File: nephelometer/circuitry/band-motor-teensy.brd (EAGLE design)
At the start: 77 x 48 mm, 25 parts, among them IC3 7805TV, J1 2.1MMJACKTHM, U1 MotA, U2 MotA

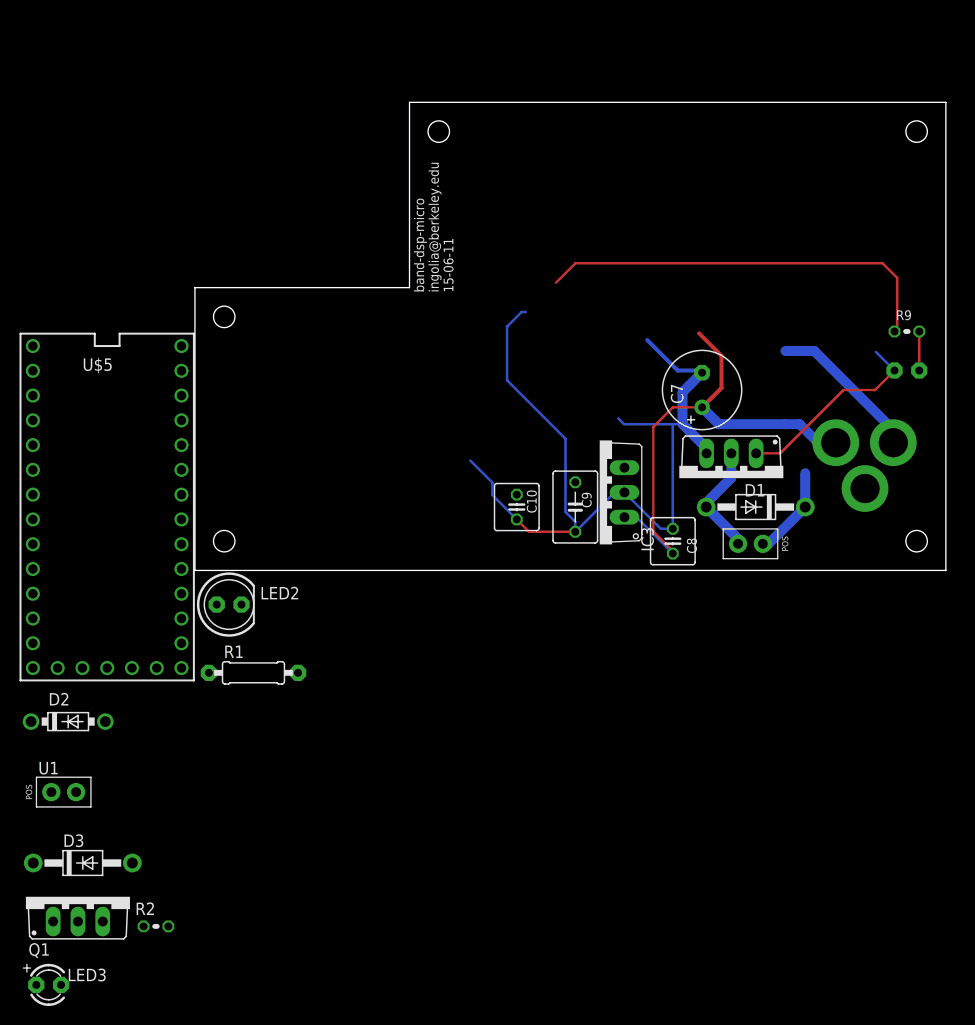
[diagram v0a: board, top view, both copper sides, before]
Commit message: Designed motor power board to stack on nephelometer or run over RJ11 cable
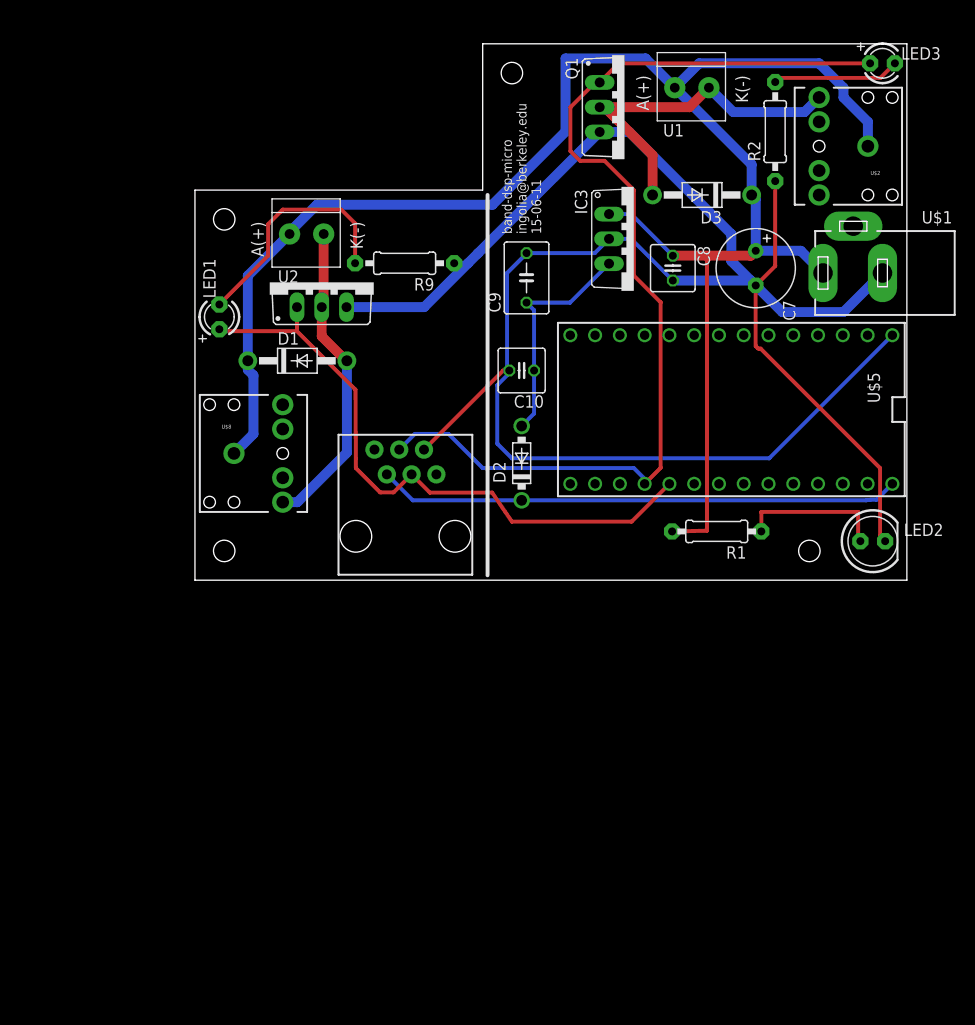
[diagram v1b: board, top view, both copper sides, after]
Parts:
- added U$6: (no value), ingolia:M2MOUNT
- added U$8: AUDIO-JACK2PTH, SparkFun-Connectors:AUDIO-JACK
- J1: value 2.1MMJACKTHM -> RJ11-6PTH; device adafruit:PJ-102A -> SparkFun-Connectors:RJ11-6
- R2, R9: device adafruit:0204V -> adafruit:0207/10
- U$1: value (none) -> PJ-102A; device ingolia:M2MOUNT -> ingolia:PJ-102A
- U$2: value (none) -> AUDIO-JACK2PTH; device ingolia:M2MOUNT -> SparkFun-Connectors:AUDIO-JACK
- U$5: value TEENSY_3.1-3.2_OUTER_ROW -> TEENSY_3.1-3.2_DIL; device Teensy_3_and_LC_Series_Boards_v1.4:TEENSY_3.0-3.2&LC_OUTER_ROW -> Teensy_3_and_LC_Series_Boards_v1.4:TEENSY_3.0-3.2&LC_DIL
- U1, U2: device ingolia:1X02_SCREW -> ingolia:1X02_3.5MM_MOT
- moved LED3 127.4 mm to (70.5, 58.0)
- moved R2 103.3 mm to (59.5, 51.0), turned to 90 degrees
- moved U1 99.5 mm to (51.0, 55.5), turned to 180 degrees
- moved Q1 99.2 mm to (41.5, 53.5), turned to 270 degrees
- moved D3 93.4 mm to (52.0, 44.5), turned to 180 degrees
- moved U$3 71.0 mm to (3.00, 8.00)
- moved LED1 70.7 mm to (2.50, 32.0), flipped to the top, turned to 90 degrees
- moved U$1 70.1 mm to (67.5, 36.5), turned to 90 degrees
- moved LED2 66.3 mm to (69.5, 9.00)
- moved U$5 64.8 mm to (55.0, 22.5), turned to 270 degrees
- moved J1 59.3 mm to (16.5, 9.50), flipped to the top, turned to 0 degrees
- moved U$7 57.4 mm to (63.0, 8.00)
- moved U2 56.9 mm to (11.5, 40.5)
- moved D2 53.5 mm to (33.5, 17.0), turned to 90 degrees
- moved R9 52.0 mm to (21.5, 37.5), turned to 180 degrees
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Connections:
- removed net N$19: LED1.A, Q3.G, U$5.17/A3
- removed net N$6: LED3.A, Q1.G, U$5.16/A2
- removed net VBAT: U$5.VBAT
- new net MOT1: J1.3, LED3.A, Q1.G, U$5.16/A2
- new net MOT2: J1.4, LED1.A, Q3.G, U$5.17/A3
- net +12V: now also U$1.1TIP, U$2.SLEEVE, U$8.SLEEVE, U1.1A, U2.1A; no longer J1.TIP, U1.1/POS, U2.1/POS
- net +5V: now also J1.2
- net 3.3V: no longer U$5.3.3V1
- net GND: now also J1.5, U$1.3RING; no longer J1.RING, U$5.GND1
- net N$3: now also U$8.TIP, U2.2K; no longer U2.2
- net N$4: now also U$2.TIP, U1.2K; no longer U1.2
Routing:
- net +12V: track 58.3 -> 181.3 mm
- net MOT1: track 0.00 -> 105.4 mm
- net GND: track 147.3 -> 222.9 mm
- net MOT2: track 0.00 -> 64.9 mm
- net +5V: track 0.00 -> 53.6 mm
- net N$4: track 0.00 -> 36.0 mm
- net N$2: track 0.00 -> 23.6 mm
- net N$3: track 11.7 -> 32.8 mm
- net N$16: track 4.00 -> 24.5 mm
- net N$19: track 20.4 -> 0.00 mm
- net N$1: track 0.00 -> 15.2 mm
- net N$5: track 0.00 -> 13.1 mm
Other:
- board size 77 x 48 mm -> 73 x 55 mm

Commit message: Motor control with transistor gating MOSFET, shutoff when disconnected
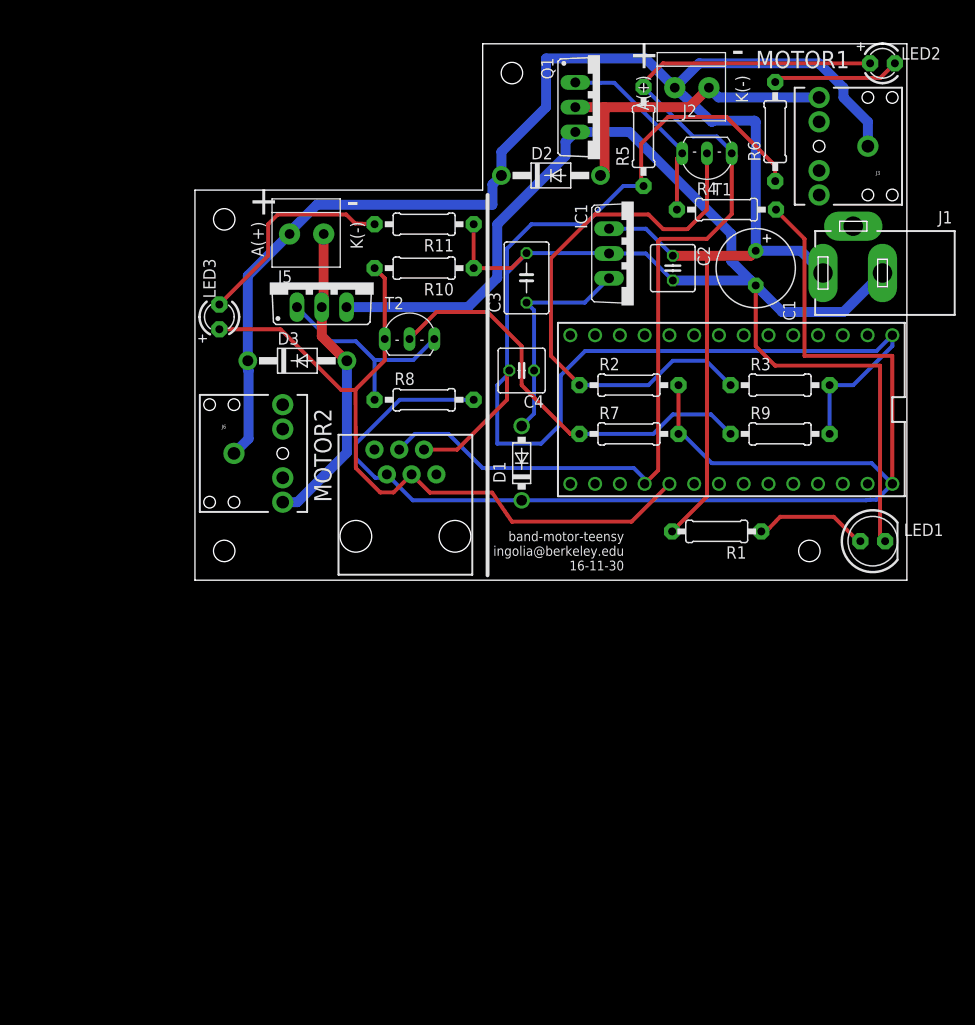
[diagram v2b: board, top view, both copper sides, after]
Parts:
- removed IC3: 7805TV, linear:TO220V
- removed U$1: PJ-102A, ingolia:PJ-102A
- added IC1: 7805TV, linear:TO220V
- added J4: RJ11-6PTH, SparkFun-Connectors:RJ11-6
- added R10, R3, R5, R7: 1K0, adafruit:0207/10
- added R11, R6: 150R, adafruit:0207/10
- added R4, R8: 4K7, adafruit:0207/10
- added T1, T2: 2N2222, adafruit:TO92-EBC-OVAL
- D1: value 1N4935 -> 1N5817-T; device adafruit:DO41-10 -> diode:DO41-7.6
- D2: value 1N5817-T -> 1N4935; device diode:DO41-7.6 -> adafruit:DO41-10
- J1: value RJ11-6PTH -> PJ-102A; device SparkFun-Connectors:RJ11-6 -> ingolia:PJ-102A
- LED1: device adafruit:LED3MM -> adafruit:LED5MM
- LED2: device adafruit:LED5MM -> adafruit:LED3MM
- R2, R9: value 150 -> 1K0
- moved LED3 72.8 mm to (2.50, 32.0), turned to 90 degrees
- moved LED1 70.8 mm to (69.5, 9.00), turned to 0 degrees
- moved J1 57.7 mm to (67.5, 36.5), turned to 90 degrees
- moved LED2 49.0 mm to (70.5, 58.0)
- moved D3 44.8 mm to (10.5, 27.5), turned to 0 degrees
- moved R9 42.3 mm to (60.0, 20.0), turned to 0 degrees
- moved R2 30.0 mm to (44.5, 25.0), turned to 0 degrees
- moved D2 29.7 mm to (36.5, 46.5), turned to 0 degrees
- moved D1 25.3 mm to (33.5, 17.0), turned to 90 degrees
- moved Q1 2.50 mm to (39.0, 53.5)
- renumbered C10 to C4, C7 to C1, C8 to C2, C9 to C3, Q3 to Q2, U$2 to J3, U$5 to MCU1, U$8 to J6, U1 to J2, U2 to J5
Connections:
- new net N$6: R2.1, R3.1, T1.B
- new net N$7: R7.1, R9.1, T2.B
- new net N$8: Q1.G, R4.1, T1.C
- new net N$9: Q2.G, R8.1, T2.C
- net +12V: now also D2.C, IC1.1, J1.1TIP; no longer D1.C, IC3.1, U$1.1TIP
- net +5V: now also D1.C, J4.2, R2.2, R4.2, R7.2, R8.2; no longer D2.C, J1.2
- net GND: now also IC1.2, J1.3RING, J4.5, LED1.K, R10.1, R11.1, R3.2, R5.1, R6.1, R9.2; no longer IC3.2, J1.5, LED2.K, R2.1, R9.1, U$1.3RING
- net MOT1: now also J4.3, LED2.A, R5.2, T1.E; no longer J1.3, LED3.A, Q1.G
- net MOT2: now also J4.4, LED3.A, R10.2, T2.E; no longer J1.4, LED1.A, Q2.G
- net N$1: now also LED1.A; no longer LED2.A
- net N$16: now also LED3.K, R11.2; no longer LED1.K, R9.2
- net N$2: now also D1.A, IC1.3; no longer D2.A, IC3.3
- net N$3: now also D3.A; no longer D1.A
- net N$4: now also D2.A; no longer D3.A
- net N$5: now also LED2.K, R6.2; no longer LED3.K, R2.2
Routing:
- net +5V: track 53.6 -> 141.2 mm
- net GND: track 222.9 -> 289.2 mm
- net N$6: track 0.00 -> 56.9 mm
- net N$7: track 0.00 -> 43.2 mm
- net N$9: track 0.00 -> 21.3 mm
- net N$8: track 0.00 -> 20.1 mm
- net MOT2: track 64.9 -> 76.6 mm
- net N$1: track 15.2 -> 11.8 mm
- net N$4: track 36.0 -> 33.4 mm
- net N$16: track 24.5 -> 22.0 mm
- net +12V: track 181.3 -> 182.3 mm
- net N$2: track 23.6 -> 23.0 mm
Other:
- board text added: "+"
- board text added: "-"
- board text added: "MOTOR1"
- board text added: "MOTOR2"
- board text added: "band-motor-teensy ingolia@berkeley.edu 16-11-30"
- board text removed: "band-dsp-micro ingolia@berkeley.edu 15-06-11"
